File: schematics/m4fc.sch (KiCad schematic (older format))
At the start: 38 parts

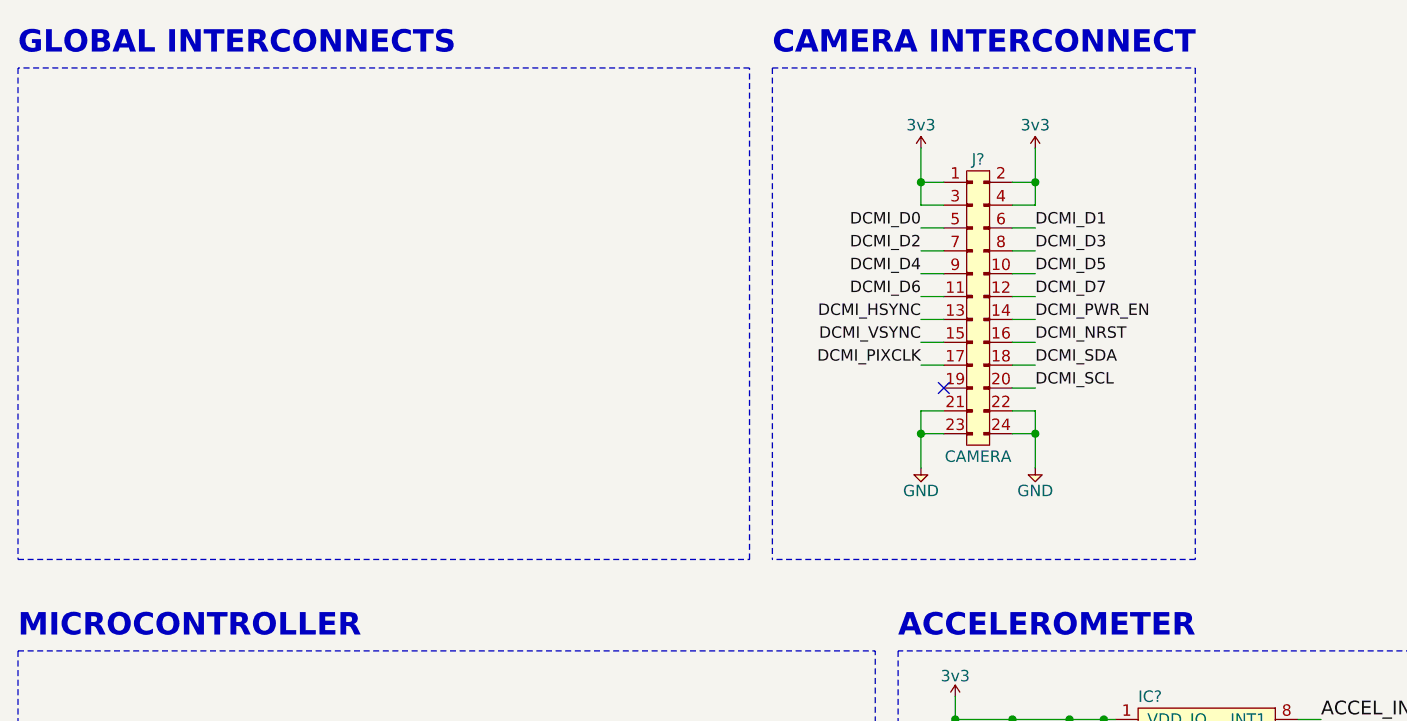
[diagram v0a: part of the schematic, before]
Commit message: Rename schematics folder and delete old board template
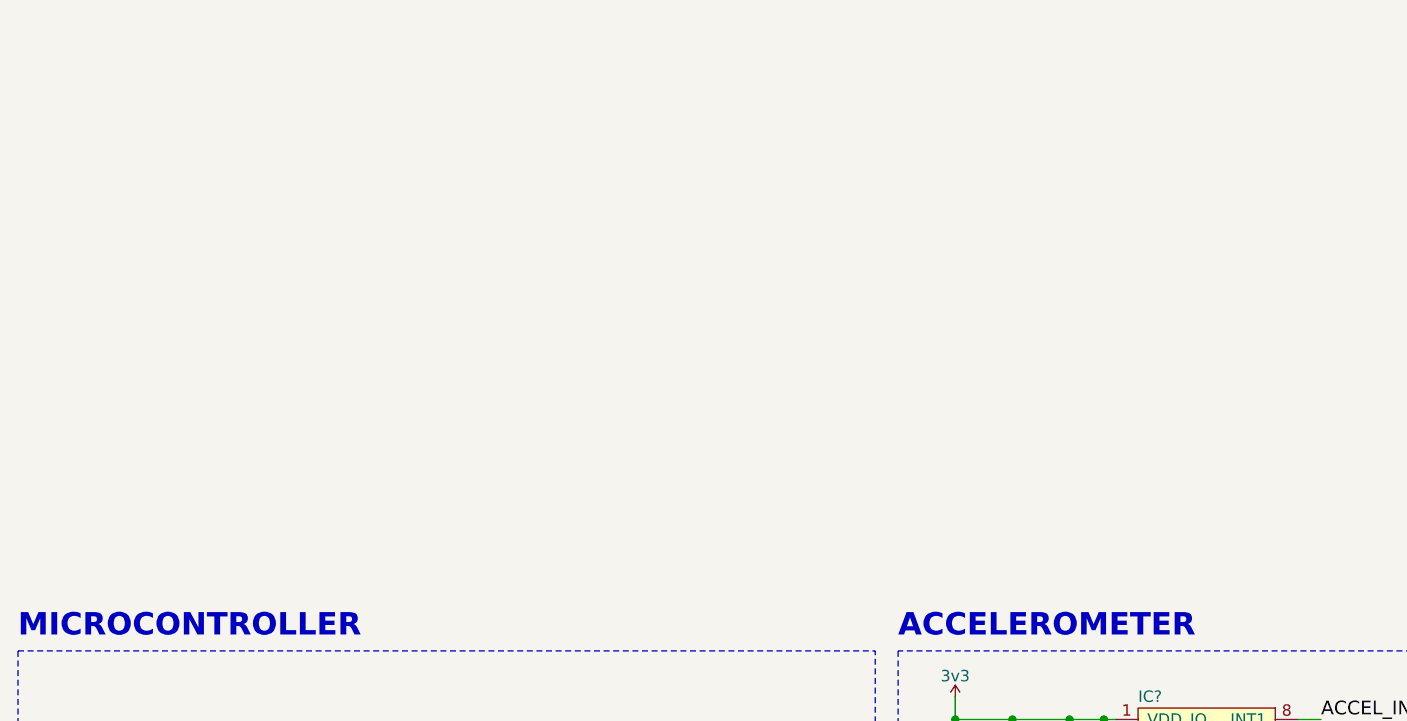
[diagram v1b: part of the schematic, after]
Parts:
- removed J?: CAMERA, symbol cusf-kicad:CONN_02x12
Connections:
- no-connect marks 4 -> 3
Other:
- note removed: "CAMERA INTERCONNECT"
- note removed: "GLOBAL INTERCONNECTS"
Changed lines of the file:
@@
 Text Label 5700 8700 0    60   ~ 0
 CAN+
-Text Notes 600  700  0    98   ~ 20
-GLOBAL INTERCONNECTS
 $Comp
 L cusf-kicad:SWD_TC P?
@@
 Text Label 5700 9200 0    60   ~ 0
 JTDR
-Wire Notes Line
-	600  2900 3800 2900
-Wire Notes Line
-	3800 2900 3800 750
-Wire Notes Line
-	3800 750  600  750
-Wire Notes Line
-	600  750  600  2900
 Wire Notes Line
 	4350 8400 600  8400
@@
 Text Notes 4450 6650 0    98   ~ 20
 BEEPER
-$Comp
-L cusf-kicad:CONN_02x12 J?
-U 1 1 5ED17754
-P 4850 1250
-F 0 "J?" H 4800 1350 50  0000 C CNN
-F 1 "CAMERA" H 4800 50  50  0000 C CNN
-F 2 "" H 4850 1250 50  0001 C CNN
-F 3 "" H 4850 1250 50  0001 C CNN
-	1    4850 1250
-	1    0    0    -1
-$EndComp
-Wire Wire Line
-	4650 1350 4550 1350
-Wire Wire Line
-	4550 1350 4550 1250
-Wire Wire Line
-	4550 1250 4650 1250
-Wire Wire Line
-	4950 1250 5050 1250
-Wire Wire Line
-	5050 1250 5050 1350
-Wire Wire Line
-	4950 1350 5050 1350
-Wire Wire Line
-	5050 1250 5050 1100
-Connection ~ 5050 1250
-Wire Wire Line
-	4550 1100 4550 1250
-Connection ~ 4550 1250
-$Comp
-L cusf-kicad:3v3 #PWR?
-U 1 1 5ED8339B
-P 4550 1100
-F 0 "#PWR?" H 4550 1210 50  0001 L CNN
-F 1 "3v3" H 4550 1200 50  0000 C CNN
-F 2 "" H 4550 1100 50  0001 C CNN
-F 3 "" H 4550 1100 50  0001 C CNN
-	1    4550 1100
-	1    0    0    -1
-$EndComp
-$Comp
-L cusf-kicad:3v3 #PWR?
-U 1 1 5ED836CE
-P 5050 1100
-F 0 "#PWR?" H 5050 1210 50  0001 L CNN
-F 1 "3v3" H 5050 1200 50  0000 C CNN
-F 2 "" H 5050 1100 50  0001 C CNN
-F 3 "" H 5050 1100 50  0001 C CNN
-	1    5050 1100
-	1    0    0    -1
-$EndComp
-Wire Wire Line
-	4650 2350 4550 2350
-Wire Wire Line
-	4550 2350 4550 2500
-Wire Wire Line
-	4550 2350 4550 2250
-Wire Wire Line
-	4550 2250 4650 2250
-Connection ~ 4550 2350
-Wire Wire Line
-	4950 2350 5050 2350
-Wire Wire Line
-	5050 2350 5050 2500
-Wire Wire Line
-	5050 2350 5050 2250
-Wire Wire Line
-	5050 2250 4950 2250
-Connection ~ 5050 2350
-$Comp
-L cusf-kicad:GND #PWR?
-U 1 1 5EDD9C20
-P 4550 2500
-F 0 "#PWR?" H 4420 2540 50  0001 L CNN
-F 1 "GND" H 4550 2400 50  0000 C CNN
-F 2 "" H 4550 2500 50  0001 C CNN
-F 3 "" H 4550 2500 50  0001 C CNN
-	1    4550 2500
-	1    0    0    -1
-$EndComp
-$Comp
-L cusf-kicad:GND #PWR?
-U 1 1 5EDDA6DE
-P 5050 2500
-F 0 "#PWR?" H 4920 2540 50  0001 L CNN
-F 1 "GND" H 5050 2400 50  0000 C CNN
-F 2 "" H 5050 2500 50  0001 C CNN
-F 3 "" H 5050 2500 50  0001 C CNN
-	1    5050 2500
-	1    0    0    -1
-$EndComp
-Wire Wire Line
-	4650 1450 4550 1450
-Wire Wire Line
-	4650 1550 4550 1550
-Wire Wire Line
-	4650 1650 4550 1650
-Wire Wire Line
-	4650 1750 4550 1750
-Wire Wire Line
-	4650 1850 4550 1850
-Wire Wire Line
-	4950 1450 5050 1450
-Wire Wire Line
-	4950 1550 5050 1550
-Wire Wire Line
-	4950 1650 5050 1650
-Wire Wire Line
-	4950 1750 5050 1750
-Wire Wire Line
-	4950 1850 5050 1850
-Wire Wire Line
-	5050 1950 4950 1950
-Wire Wire Line
-	5050 2050 4950 2050
-Wire Wire Line
-	4550 2050 4650 2050
-Wire Wire Line
-	4550 1950 4650 1950
-Text Label 5050 1450 0    50   ~ 0
-DCMI_D1
-Text Label 5050 1550 0    50   ~ 0
-DCMI_D3
-Text Label 5050 1650 0    50   ~ 0
-DCMI_D5
-Text Label 5050 1750 0    50   ~ 0
-DCMI_D7
-Text Label 4550 1750 2    50   ~ 0
-DCMI_D6
-Text Label 4550 1650 2    50   ~ 0
-DCMI_D4
-Text Label 4550 1550 2    50   ~ 0
-DCMI_D2
-Text Label 4550 1450 2    50   ~ 0
-DCMI_D0
-Text Label 4550 2050 2    50   ~ 0
-DCMI_PIXCLK
-Text Label 4550 1950 2    50   ~ 0
-DCMI_VSYNC
-Text Label 4550 1850 2    50   ~ 0
-DCMI_HSYNC
-Text Label 5050 1850 0    50   ~ 0
-DCMI_PWR_EN
-Text Label 5050 1950 0    50   ~ 0
-DCMI_NRST
-Wire Notes Line
-	3900 750  5750 750
-Wire Notes Line
-	5750 750  5750 2900
-Wire Notes Line
-	5750 2900 3900 2900
-Wire Notes Line
-	3900 750  3900 2900
-Text Notes 3900 700  0    98   ~ 20
-CAMERA INTERCONNECT
-Wire Wire Line
-	4950 2150 5050 2150
-Text Label 5050 2050 0    50   ~ 0
-DCMI_SDA
-Text Label 5050 2150 0    50   ~ 0
-DCMI_SCL
-NoConn ~ 4650 2150
 Wire Wire Line
 	5550 8800 5700 8800

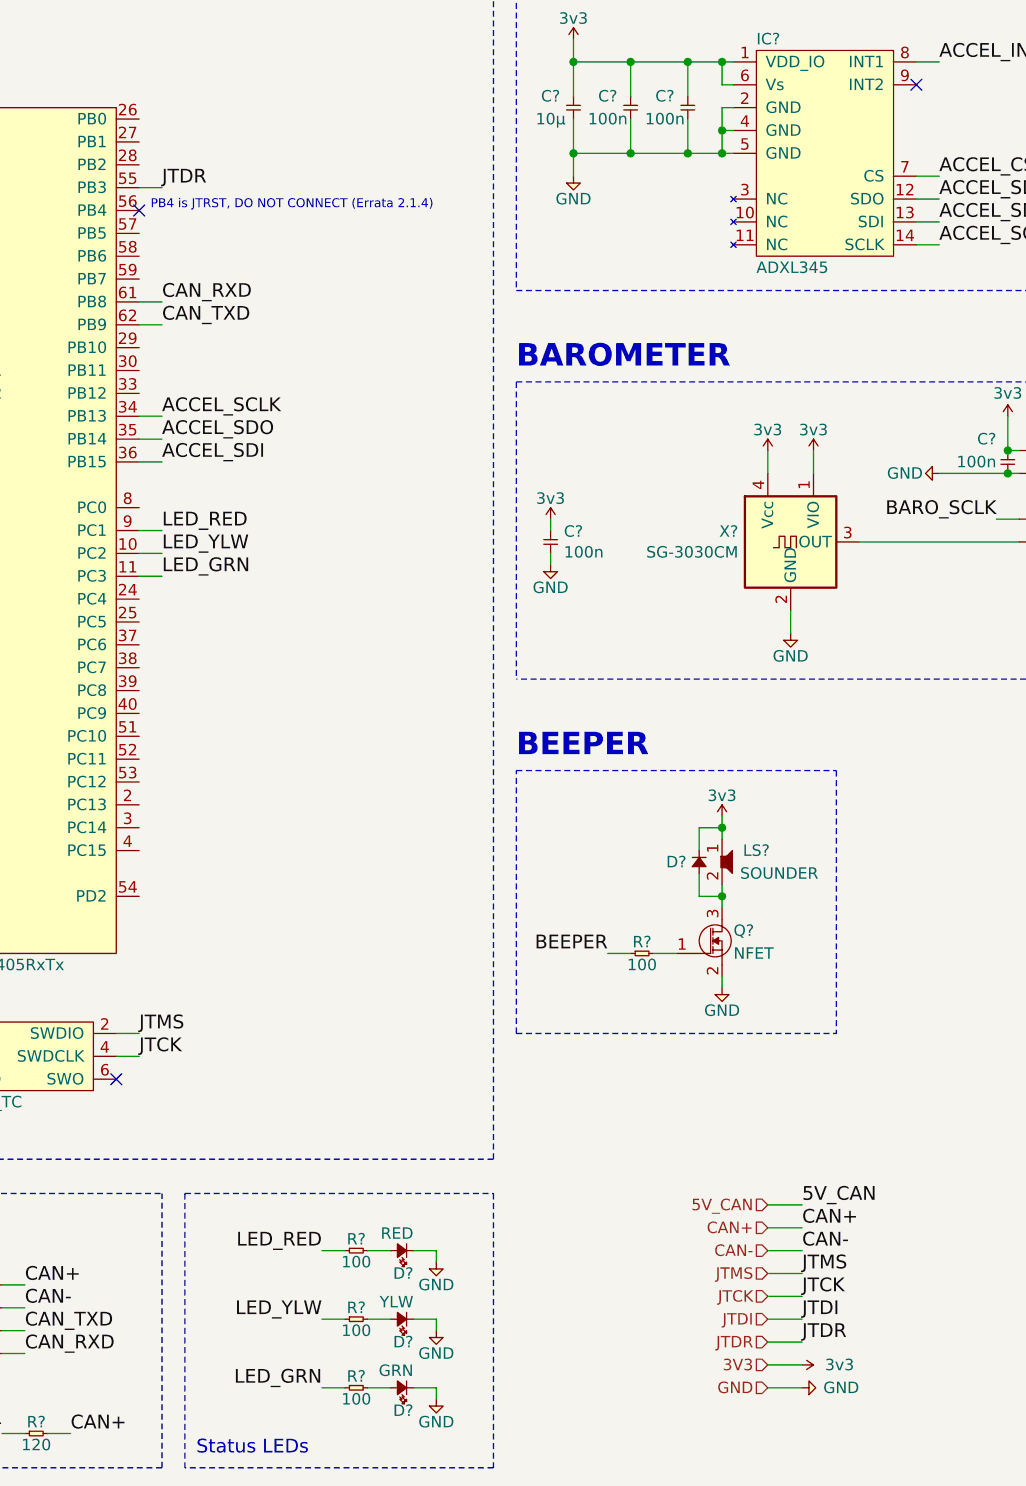
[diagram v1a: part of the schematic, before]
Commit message: Chain JTAG connections
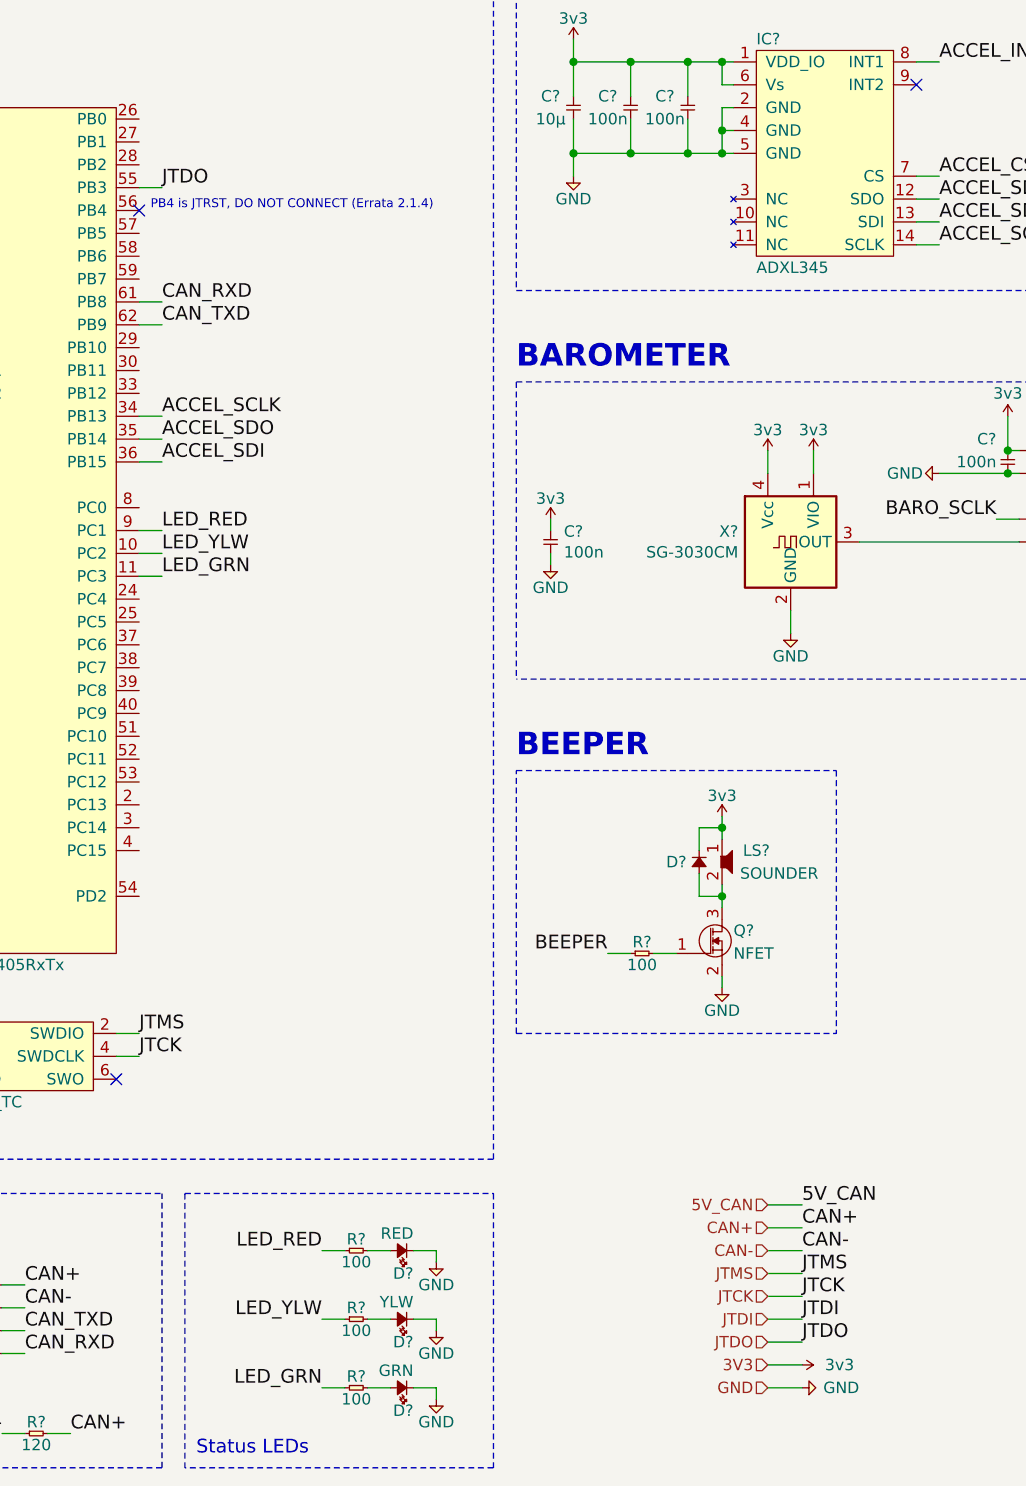
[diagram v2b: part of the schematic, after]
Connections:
- net JTDR renamed JTDO
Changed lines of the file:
@@
 JTDI
 Text Label 2900 4150 0    60   ~ 0
-JTDR
+JTDO
 Text Label 5700 8900 0    60   ~ 0
 JTMS
@@
 CAN_RXD
 Text Label 5700 9200 0    60   ~ 0
-JTDR
+JTDO
 Wire Notes Line
 	4350 8400 600  8400
@@
 JTDI
 Text HLabel 5550 9200 0    50   Input ~ 0
-JTDR
+JTDO
 Text HLabel 5550 9300 0    50   Input ~ 0
 3V3
